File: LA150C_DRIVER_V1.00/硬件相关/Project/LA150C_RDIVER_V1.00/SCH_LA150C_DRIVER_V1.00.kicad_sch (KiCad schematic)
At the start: 23 parts, among them U4 MP6543HGL-Z

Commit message: chore: save LA150C schematic updates
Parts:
- removed C19: 10uF, Capacitors:C1210, symbol LA150C_RDIVER_V1.00:GRM32EC72A106KE05L
- removed C27: 100nF, Capacitors:C0201, symbol LA150C_RDIVER_V1.00:GRM033Z71C104KE14D
- removed R32: 10K, Resistors:R0201, symbol LA150C_RDIVER_V1.00:RC0201FR-0710KL
- added C23: 1uF, Capacitors:C0603, symbol Capacitors:GRM188D72A105KE01D
- added C30: 100nF, Capacitors:C0201, symbol LA150C_RDIVER_V1.00:GRM033Z71C104KE14D
- added R20: 10K, Resistors:R0201, symbol LA150C_RDIVER_V1.00:RC0201FR-0710KL
- renumbered C24 to C22, C20 to C24, C22 to C26, C21 to C27, C23 to C28, C26 to C29, R26 to R10, R23 to R11, R29 to R12, R27 to R13, R24 to R14, R22 to R15, R30 to R16, R28 to R17, R25 to R18, R31 to R19, U4 to U3
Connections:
- net AD_NTC: now also C30.1, R20.1
- net AGND: now also C30.2, R20.2
- net PGND: now also C23.2
- net VBUS: now also C23.1
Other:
- moved on the sheet: C24, C26, C27, C28, FB1, R15, U3

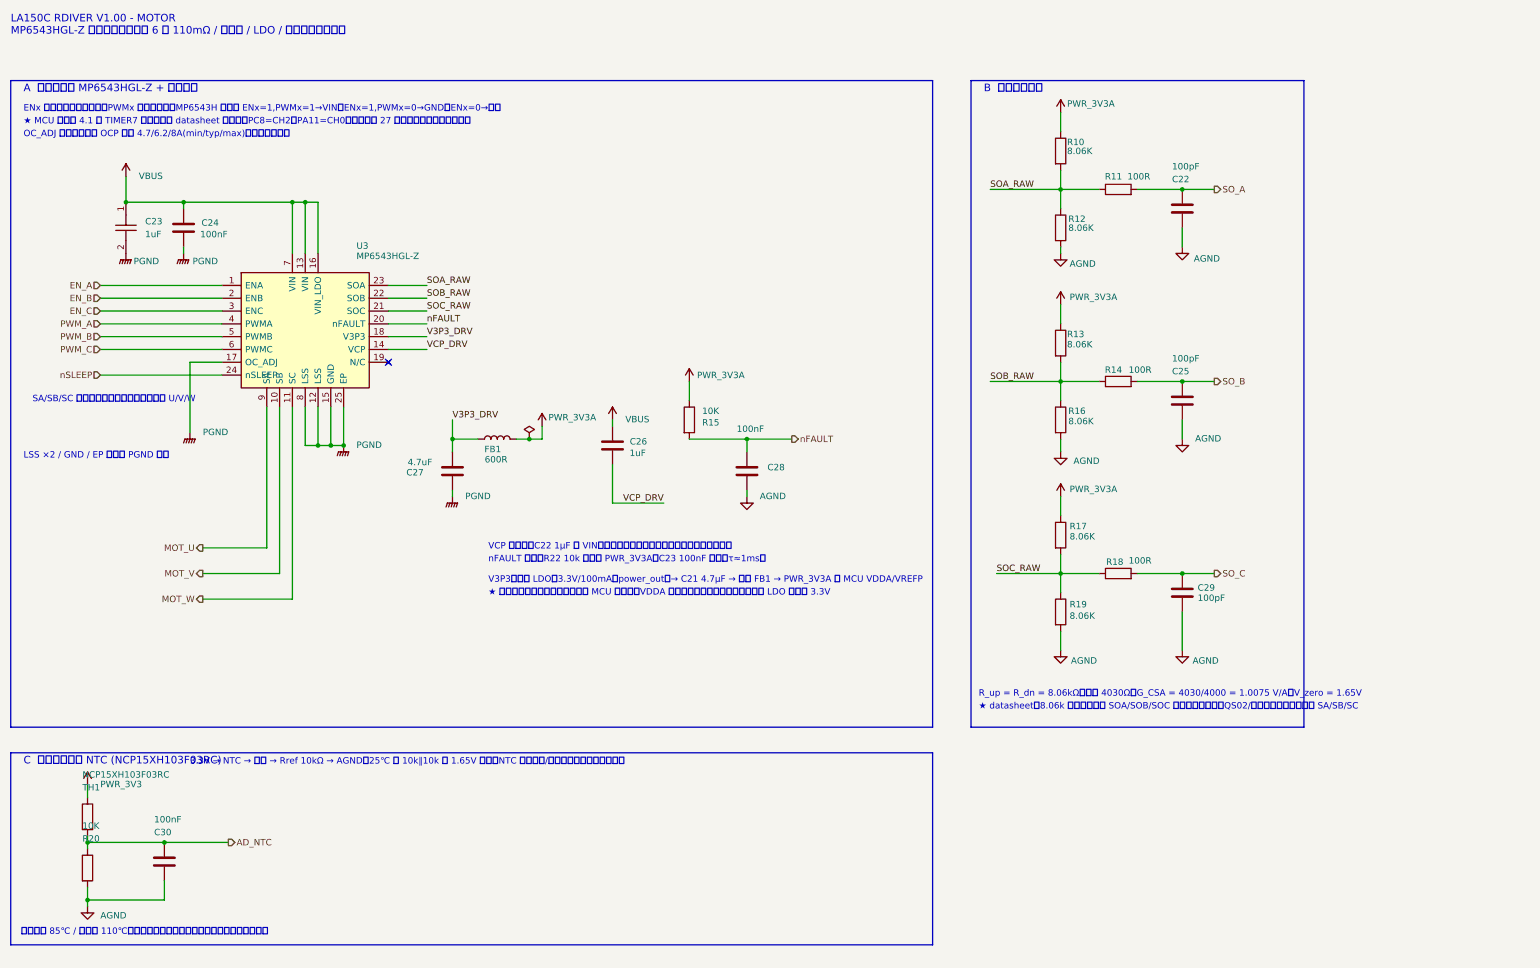
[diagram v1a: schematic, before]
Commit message: feat: finalize LA150C driver schematic
Align the GD32F503 BGA64 pin resources with QS01 V1.12, retain the SCT2230, MT6701 and CAN FD circuits, replace the motor test points with 1.0 x 2.0 mm solder pads, and update the symbols, footprints, ERC report, netlist, BOM and PDF.
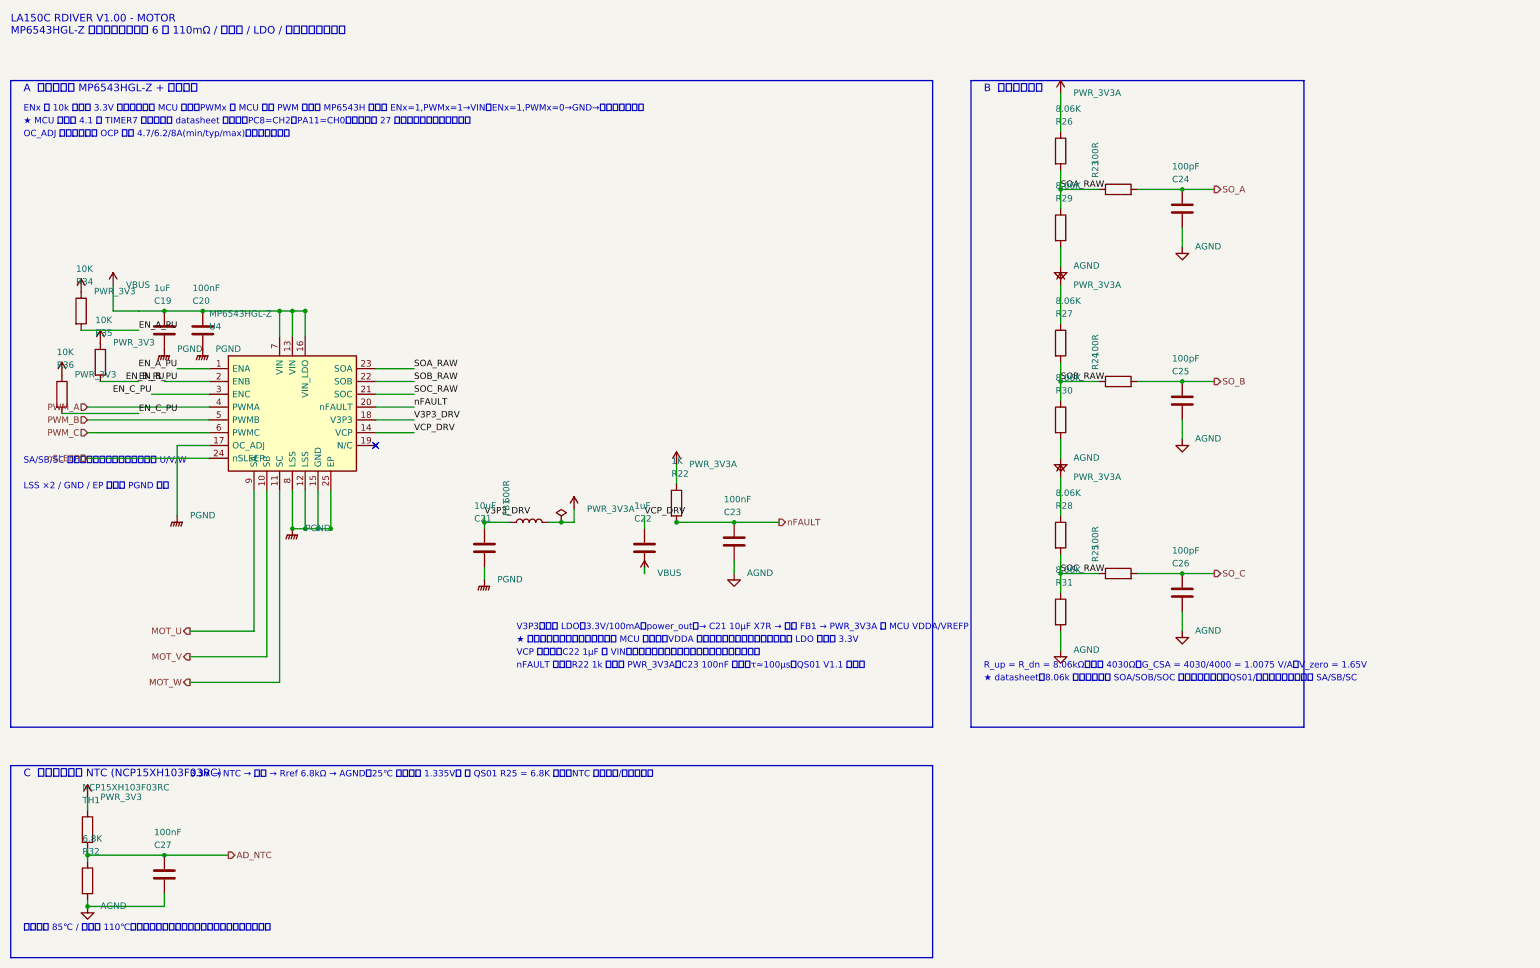
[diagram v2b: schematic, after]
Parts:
- removed C23: 1uF, Capacitors:C0603, symbol Capacitors:GRM188D72A105KE01D
- removed C30: 100nF, Capacitors:C0201, symbol LA150C_RDIVER_V1.00:GRM033Z71C104KE14D
- removed R20: 10K, Resistors:R0201, symbol LA150C_RDIVER_V1.00:RC0201FR-0710KL
- added C19: 1uF, Capacitors:C_0603_1608Metric, symbol LA150C_RDIVER_V1.00:CL10B105KB8NQNC
- added C27: 100nF, Capacitors:C0201, symbol LA150C_RDIVER_V1.00:GRM033Z71C104KE14D
- added R32: 6.8K, Resistors:R0201, symbol LA150C_RDIVER_V1.00:RC0201FR-076K8L
- added R34, R35, R36: 10K, Resistors:R0201, symbol LA150C_RDIVER_V1.00:RC0201FR-0710KL
- C21: renamed from C27; value 4.7uF -> 10uF; footprint Capacitors:C0603 -> Capacitors:C_0603_1608Metric; symbol LA150C_RDIVER_V1.00:CL10A475KP8NNNC -> LA150C_RDIVER_V1.00:GRM188Z71A106KA73D; LCSC Part C1705 -> C2959727; MPN CL10A475KP8NNNC -> GRM188Z71A106KA73D; Manufacturer SAMSUNG(三星) -> muRata(村田)
- C22: renamed from C26; Manufacturer SAMSUNG(三星) -> Samsung Electro-Mechanics
- C24: renamed from C22; footprint Capacitors:C_0201_0603Metric -> Capacitors:C0201; symbol LA150C_RDIVER_V1.00:FN03N100J500PLG -> LA150C_RDIVER_V1.00:CL03C101JB3NNNC; LCSC Part C561710 -> C730413; MPN FN03N100J500PLG -> CL03C101JB3NNNC; Manufacturer PSA -> Samsung Electro-Mechanics
- C25: footprint Capacitors:C_0201_0603Metric -> Capacitors:C0201; symbol LA150C_RDIVER_V1.00:FN03N100J500PLG -> LA150C_RDIVER_V1.00:CL03C101JB3NNNC; LCSC Part C561710 -> C730413; MPN FN03N100J500PLG -> CL03C101JB3NNNC; Manufacturer PSA -> Samsung Electro-Mechanics
- C26: renamed from C29; footprint Capacitors:C_0201_0603Metric -> Capacitors:C0201; symbol LA150C_RDIVER_V1.00:FN03N100J500PLG -> LA150C_RDIVER_V1.00:CL03C101JB3NNNC; LCSC Part C561710 -> C730413; MPN FN03N100J500PLG -> CL03C101JB3NNNC; Manufacturer PSA -> Samsung Electro-Mechanics
- R22: renamed from R15; value 10K -> 1K; symbol LA150C_RDIVER_V1.00:RC0201FR-0710KL -> LA150C_RDIVER_V1.00:RC0201FR-071KL; LCSC Part C106225 -> C138165; MPN RC0201FR-0710KL -> RC0201FR-071KL; Manufacturer YAGEO(国巨) -> YAGEO
- renumbered C24 to C20, C28 to C23, R11 to R23, R14 to R24, R18 to R25, R10 to R26, R13 to R27, R17 to R28, R12 to R29, R16 to R30, R19 to R31, U3 to U4
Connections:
- net AD_NTC: now also C27.1, R32.1
- net AGND: now also C27.2, R32.2
- net PGND: now also C19.2
- net PWR_3V3: now also R34.1, R35.1, R36.1
- net VBUS: now also C19.1
- net EN_A renamed EN_A_PU
- net EN_A_PU: now also R34.2
- net EN_B renamed EN_B_PU
- net EN_B_PU: now also R35.2
- net EN_C renamed EN_C_PU
- net EN_C_PU: now also R36.2
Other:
- note added: "3.3V → NTC → 节点 → Rref 6.8kΩ → AGND；25℃ 时节点约 1.335V。 按 QS01 R25 = 6.8K 修改，NTC 位于电机/丝杠内部。"
- note added: "ENx 由 10k 上拉到 3.3V 常使能，不由 MCU 控制；PWMx 由 MCU 三相 PWM 驱动。 MP6543H 真值表 ENx=1,PWMx=1→VIN；ENx=1,PWMx=0→GND→内部互补输出。"
- note added: "V3P3（内部 LDO，3.3V/100mA，power_out）→ C21 10µF X7R → 磁珠 FB1 → PWR_3V3A 供 MCU VDDA/VREFP"
- note added: "nFAULT 开漏：R22 1k 上拉到 PWR_3V3A，C23 100nF 去抖（τ≈100µs，QS01 V1.1 口径）"
- note added: "★ datasheet：8.06k 端接网络接在 SOA/SOB/SOC 电流采样输出上；QS01/工程文档把它误写为 SA/SB/SC"
- note removed: "3.3V → NTC → 节点 → Rref 10kΩ → AGND；25℃ 时 10k‖10k 得 1.65V 中点。NTC 位于电机/丝杠内部，经内部线束接入"
- note removed: "ENx 为使能（内部下拉），PWMx 为斩波输入；MP6543H 真值表 ENx=1,PWMx=1→VIN；ENx=1,PWMx=0→GND；ENx=0→高阻"
- note removed: "V3P3（内部 LDO，3.3V/100mA，power_out）→ C21 4.7µF → 磁珠 FB1 → PWR_3V3A 供 MCU VDDA/VREFP"
- note removed: "nFAULT 开漏：R22 10k 上拉到 PWR_3V3A，C23 100nF 去抖（τ≈1ms）"
- note removed: "★ datasheet：8.06k 端接网络接在 SOA/SOB/SOC 电流采样输出上；QS02/本工程文档把它误写为 SA/SB/SC"
- moved on the sheet: C20, C21, C22, C23, FB1, R22, U4
